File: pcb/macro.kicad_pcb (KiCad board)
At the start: 2 copper layers, 85.5 x 64.2 mm, 21 parts, among them K1 KEYSW, K2 KEYSW, K3 KEYSW, K4 KEYSW, K5 KEYSW, K6 KEYSW, U1 ProMicro

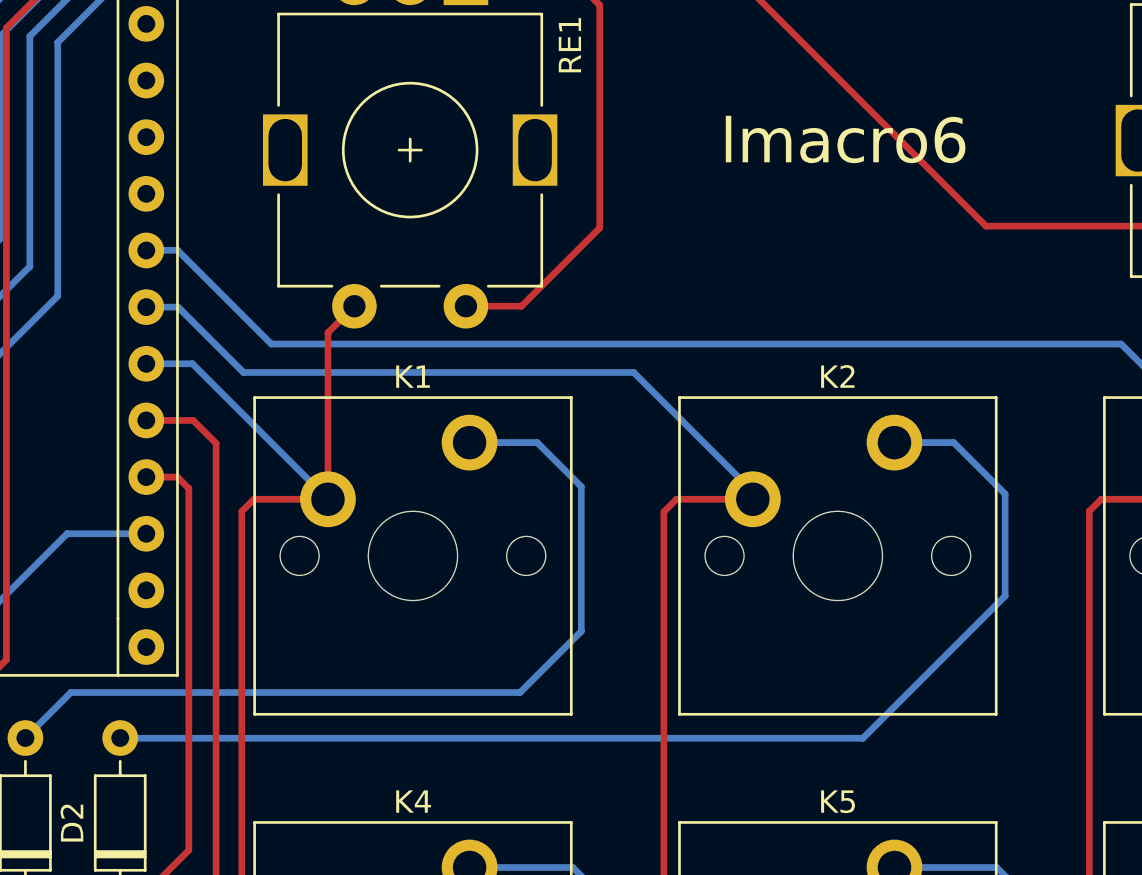
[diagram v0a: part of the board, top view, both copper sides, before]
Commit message: feat: add button switch for reset
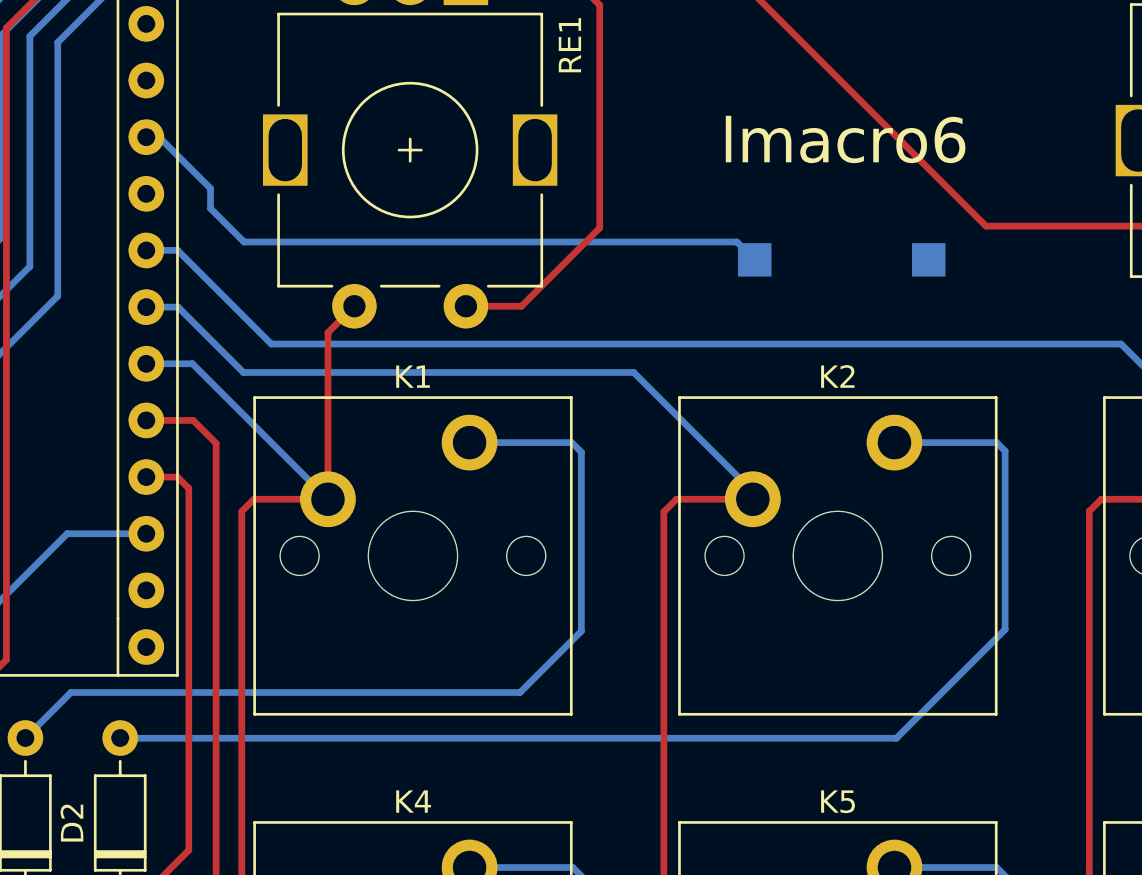
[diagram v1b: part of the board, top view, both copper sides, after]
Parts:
- added SW1: SW_Push, Button_Switch_SMD:SW_SPST_CK_RS282G05A3, B.Cu at (104.1, 101.1)
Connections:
- U1 pad 22: unconnected-(U1-Pad22) -> Net-(U1-Pad22)
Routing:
- net Net-(U1-Pad22): track 0.00 -> 30.1 mm
- net Net-(D2-Pad2): track 52.0 -> 54.1 mm
- net Net-(D1-Pad2): track 39.2 -> 40.1 mm
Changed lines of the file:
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@@
   (net 24 "unconnected-(U1-Pad14)")
   (net 25 "unconnected-(U1-Pad21)")
-  (net 26 "unconnected-(U1-Pad22)")
+  (net 26 "Net-(U1-Pad22)")
   (net 27 "unconnected-(U1-Pad24)")
   (net 28 "Net-(D2-Pad2)")
@@
       (net 25 "unconnected-(U1-Pad21)") (pinfunction "VCC") (pintype "power_in"))
     (pad "22" thru_hole oval locked (at 0 22.86 180) (size 1.6 1.6) (drill 0.8) (layers *.Cu *.Mask)
-      (net 26 "unconnected-(U1-Pad22)") (pinfunction "RST") (pintype "input"))
+      (net 26 "Net-(U1-Pad22)") (pinfunction "RST") (pintype "input"))
     (pad "23" thru_hole oval locked (at 0 25.4 180) (size 1.6 1.6) (drill 0.8) (layers *.Cu *.Mask)
       (net 16 "GND") (pinfunction "GND") (pintype "power_in"))
@@
     )
   )
+  (footprint "Button_Switch_SMD:SW_SPST_CK_RS282G05A3" (layer "B.Cu")
+    (at 104.1 101.1)
+    (descr "https://www.mouser.com/ds/2/60/RS-282G05A-SM_RT-1159762.pdf")
+    (tags "SPST button tactile switch")
+    (property "Sheetfile" "macro.kicad_sch")
+    (property "Sheetname" "")
+    (attr smd)
+    (fp_text reference "SW1" (at 0 2.6) (layer "B.SilkS")
+      (effects (font (size 1 1) (thickness 0.15)) (justify mirror))
+    )
+    (fp_text value "SW_Push" (at 0 -3) (layer "B.Fab")
+      (effects (font (size 1 1) (thickness 0.15)) (justify mirror))
+    )
+    (fp_text user "${REFERENCE}" (at 0 2.6) (layer "B.Fab")
+      (effects (font (size 1 1) (thickness 0.15)) (justify mirror))
+    )
+    (fp_line (start 3.06 -1.85) (end -3.06 -1.85) (layer "B.SilkS") (width 0.12))
+    (fp_line (start -3.06 -1.85) (end -3.06 1.85) (layer "B.SilkS") (width 0.12))
+    (fp_line (start -3.06 1.85) (end 3.06 1.85) (layer "B.SilkS") (width 0.12))
+    (fp_line (start 3.06 1.85) (end 3.06 -1.85) (layer "B.SilkS") (width 0.12))
+    (fp_line (start -4.9 -2.05) (end -4.9 2.05) (layer "B.CrtYd") (width 0.05))
+    (fp_line (start 4.9 -2.05) (end -4.9 -2.05) (layer "B.CrtYd") (width 0.05))
+    (fp_line (start 4.9 2.05) (end 4.9 -2.05) (layer "B.CrtYd") (width 0.05))
+    (fp_line (start -4.9 2.05) (end 4.9 2.05) (layer "B.CrtYd") (width 0.05))
+    (fp_line (start 1.5 0.8) (end 1.5 -0.8) (layer "B.Fab") (width 0.1))
+    (fp_line (start -1.5 0.8) (end -1.5 -0.8) (layer "B.Fab") (width 0.1))
+    (fp_line (start 1.75 -1) (end -1.75 -1) (layer "B.Fab") (width 0.1))
+    (fp_line (start -1.75 -1) (end -1.75 1) (layer "B.Fab") (width 0.1))
+    (fp_line (start -1.75 1) (end 1.75 1) (layer "B.Fab") (width 0.1))
+    (fp_line (start 1.75 1) (end 1.75 -1) (layer "B.Fab") (width 0.1))
+    (fp_line (start -1.5 -0.8) (end 1.5 -0.8) (layer "B.Fab") (width 0.1))
+    (fp_line (start 3 1.8) (end 3 -1.8) (layer "B.Fab") (width 0.1))
+    (fp_line (start -1.5 0.8) (end 1.5 0.8) (layer "B.Fab") (width 0.1))
+    (fp_line (start -3 -1.8) (end 3 -1.8) (layer "B.Fab") (width 0.1))
+    (fp_line (start -3 1.8) (end 3 1.8) (layer "B.Fab") (width 0.1))
+    (fp_line (start -3 1.8) (end -3 -1.8) (layer "B.Fab") (width 0.1))
+    (pad "1" smd rect (at -3.9 0) (size 1.5 1.5) (layers "B.Cu" "B.Paste" "B.Mask")
+      (net 26 "Net-(U1-Pad22)") (pinfunction "1") (pintype "passive"))
+    (pad "2" smd rect (at 3.9 0) (size 1.5 1.5) (layers "B.Cu" "B.Paste" "B.Mask")
+      (net 16 "GND") (pinfunction "2") (pintype "passive"))
+    (model "${KICAD6_3DMODEL_DIR}/Button_Switch_SMD.3dshapes/SW_SPST_CK_RS282G05A3.wrl"
+      (offset (xyz 0 0 0))
+      (scale (xyz 1 1 1))
+      (rotate (xyz 0 0 0))
+    )
+  )
   (gr_circle (center 122.98 95.75) (end 123.16 95.58) (layer "Dwgs.User") (width 0.15) (fill none))
   (gr_circle (center 84.75 96.18) (end 84.91 96.05) (layer "Dwgs.User") (width 0.15) (fill none))
@@
   (segment (start 67.5 131.23) (end 67.5 130.16) (width 0.3) (layer "B.Cu") (net 1))
   (segment (start 69.54 120.5) (end 89.675 120.5) (width 0.3) (layer "B.Cu") (net 2))
-  (segment (start 92.425 117.75) (end 92.425 111.275) (width 0.3) (layer "B.Cu") (net 2))
+  (segment (start 92.425 109.725) (end 91.995 109.295) (width 0.3) (layer "B.Cu") (net 2))
+  (segment (start 92.425 117.75) (end 92.425 109.725) (width 0.3) (layer "B.Cu") (net 2))
+  (segment (start 67.5 122.54) (end 69.54 120.5) (width 0.3) (layer "B.Cu") (net 2))
+  (segment (start 91.995 109.295) (end 87.415 109.295) (width 0.3) (layer "B.Cu") (net 2))
   (segment (start 89.675 120.5) (end 92.425 117.75) (width 0.3) (layer "B.Cu") (net 2))
-  (segment (start 90.445 109.295) (end 87.415 109.295) (width 0.3) (layer "B.Cu") (net 2))
-  (segment (start 92.425 111.275) (end 90.445 109.295) (width 0.3) (layer "B.Cu") (net 2))
-  (segment (start 67.5 122.54) (end 69.54 120.5) (width 0.3) (layer "B.Cu") (net 2))
   (segment (start 62.405 145.1) (end 122.65 145.1) (width 0.3) (layer "B.Cu") (net 3))
   (segment (start 58.975 141.67) (end 62.405 145.1) (width 0.3) (layer "B.Cu") (net 3))
@@
   (segment (start 63.3 103.225) (end 66.4 100.125) (width 0.3) (layer "B.Cu") (net 18))
   (segment (start 71.42 86.03) (end 118.257588 86.03) (width 0.3) (layer "B.Cu") (net 18))
-  (segment (start 105.05 122.55) (end 111.425 116.175) (width 0.3) (layer "B.Cu") (net 28))
-  (segment (start 111.425 116.175) (end 111.425 111.6) (width 0.3) (layer "B.Cu") (net 28))
-  (segment (start 72.51 122.55) (end 105.05 122.55) (width 0.3) (layer "B.Cu") (net 28))
-  (segment (start 109.12 109.295) (end 106.465 109.295) (width 0.3) (layer "B.Cu") (net 28))
-  (segment (start 111.425 111.6) (end 109.12 109.295) (width 0.3) (layer "B.Cu") (net 28))
+  (segment (start 77.3 100.3) (end 99.4 100.3) (width 0.3) (layer "B.Cu") (net 26))
+  (segment (start 72.92 95.6) (end 73.5 95.6) (width 0.3) (layer "B.Cu") (net 26))
+  (segment (start 73.5 95.6) (end 75.8 97.9) (width 0.3) (layer "B.Cu") (net 26))
+  (segment (start 99.4 100.3) (end 100.2 101.1) (width 0.3) (layer "B.Cu") (net 26))
+  (segment (start 75.8 98.8) (end 77.3 100.3) (width 0.3) (layer "B.Cu") (net 26))
+  (segment (start 75.8 97.9) (end 75.8 98.8) (width 0.3) (layer "B.Cu") (net 26))
+  (segment (start 111.425 117.675) (end 111.425 109.675) (width 0.3) (layer "B.Cu") (net 28))
+  (segment (start 111.045 109.295) (end 106.465 109.295) (width 0.3) (layer "B.Cu") (net 28))
+  (segment (start 106.55 122.55) (end 111.425 117.675) (width 0.3) (layer "B.Cu") (net 28))
+  (segment (start 111.425 109.675) (end 111.045 109.295) (width 0.3) (layer "B.Cu") (net 28))
+  (segment (start 72.51 122.55) (end 106.55 122.55) (width 0.3) (layer "B.Cu") (net 28))
   (zone (net 16) (net_name "GND") (layer "B.Cu") (hatch edge 0.508)
     (connect_pads (clearance 0.508))

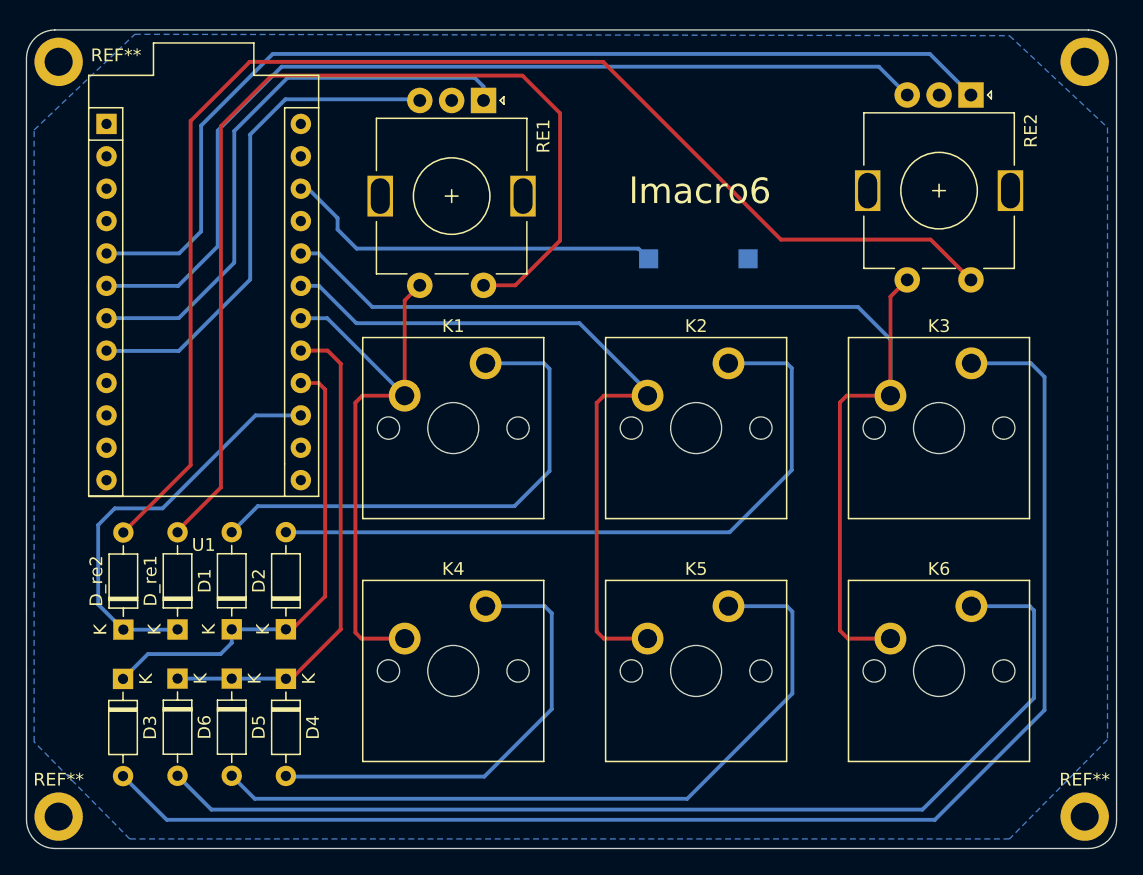
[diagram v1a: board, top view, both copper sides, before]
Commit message: fix: align rotary encoders.
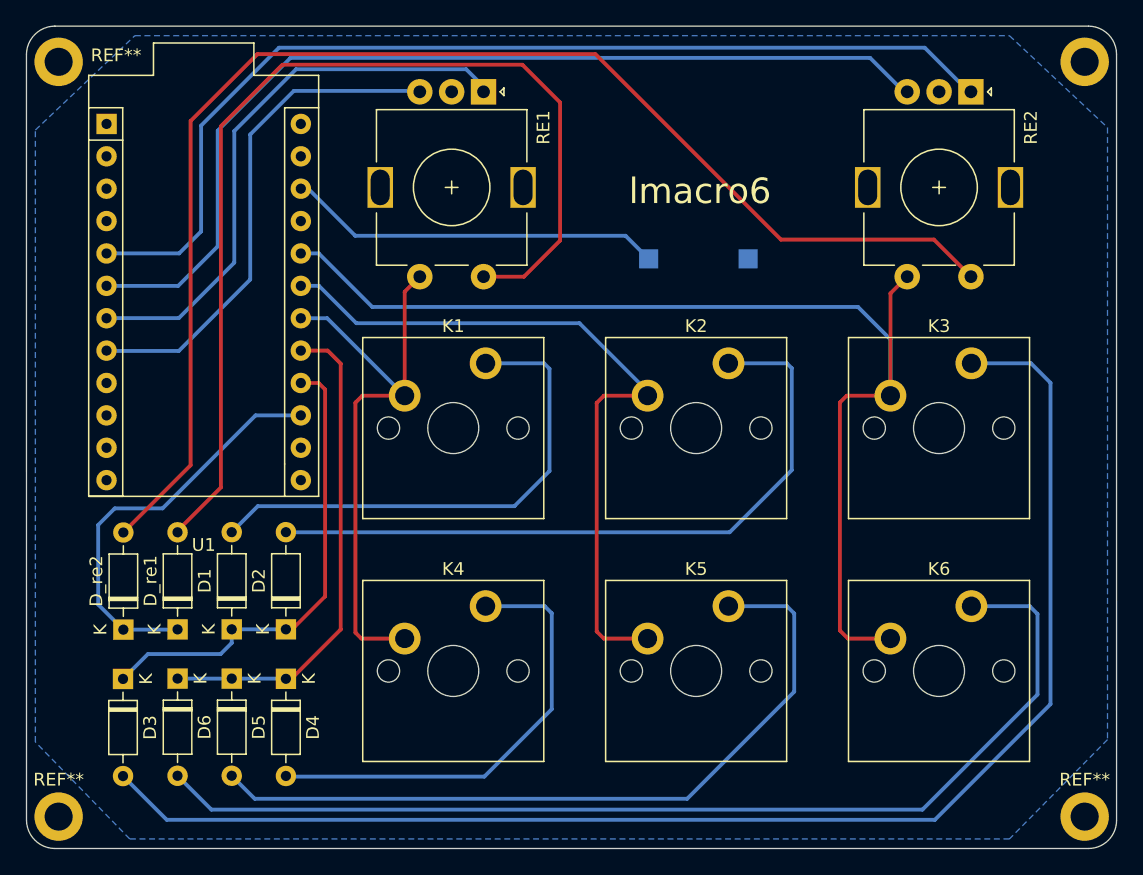
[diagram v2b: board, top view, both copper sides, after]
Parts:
- moved RE1 0.68 mm to (87.2, 88.0)
- moved RE2 0.25 mm to (125.5, 88.0)
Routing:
- net col0: track 46.0 -> 46.7 mm
- net ENC2B: track 76.2 -> 76.7 mm
- net ENC1A: track 44.8 -> 45.4 mm
- net Net-(U1-Pad22): track 30.1 -> 29.6 mm
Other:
- board size 85.5 x 64.2 mm -> 85.5 x 64.5 mm
